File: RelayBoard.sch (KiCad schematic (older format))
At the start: 12 parts

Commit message: Added A New Componet to Relay Lib
* A dioded relay
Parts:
- removed RE1, RE10, RE11, RE12, RE2, RE3, RE4, RE5, RE6, RE7, RE8, RE9: SPST-Relay, symbol SPST-Relay
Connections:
- net labels removed: VCC
- wire segments 15 -> 0
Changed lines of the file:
@@
 LIBS:valves
 LIBS:RelayLib
+LIBS:RelayBoard-cache
 EELAYER 24 0
 EELAYER END
@@
 Comment4 ""
 $EndDescr
-$Comp
-L SPST-Relay RE1
-U 1 1 54E13EE5
-P 1850 1950
-F 0 "RE1" H 1850 1650 60  0000 C CNN
-F 1 "SPST-Relay" H 1850 1850 60  0000 C CNN
-F 2 "" H 1850 1950 60  0000 C CNN
-F 3 "" H 1850 1950 60  0000 C CNN
-	1    1850 1950
-	1    0    0    -1
-$EndComp
-$Comp
-L SPST-Relay RE2
-U 1 1 54E13F01
-P 3150 1950
-F 0 "RE2" H 3150 1650 60  0000 C CNN
-F 1 "SPST-Relay" H 3150 1850 60  0000 C CNN
-F 2 "" H 3150 1950 60  0000 C CNN
-F 3 "" H 3150 1950 60  0000 C CNN
-	1    3150 1950
-	1    0    0    -1
-$EndComp
-$Comp
-L VCC #PWR1
-U 1 1 54E13F0E
-P 800 1650
-F 0 "#PWR1" H 800 1750 30  0001 C CNN
-F 1 "VCC" H 800 1750 30  0000 C CNN
-F 2 "" H 800 1650 60  0000 C CNN
-F 3 "" H 800 1650 60  0000 C CNN
-	1    800  1650
-	1    0    0    -1
-$EndComp
-$Comp
-L SPST-Relay RE3
-U 1 1 54E13F53
-P 4450 1950
-F 0 "RE3" H 4450 1650 60  0000 C CNN
-F 1 "SPST-Relay" H 4450 1850 60  0000 C CNN
-F 2 "" H 4450 1950 60  0000 C CNN
-F 3 "" H 4450 1950 60  0000 C CNN
-	1    4450 1950
-	1    0    0    -1
-$EndComp
-$Comp
-L SPST-Relay RE4
-U 1 1 54E13F5E
-P 5750 1950
-F 0 "RE4" H 5750 1650 60  0000 C CNN
-F 1 "SPST-Relay" H 5750 1850 60  0000 C CNN
-F 2 "" H 5750 1950 60  0000 C CNN
-F 3 "" H 5750 1950 60  0000 C CNN
-	1    5750 1950
-	1    0    0    -1
-$EndComp
-$Comp
-L SPST-Relay RE5
-U 1 1 54E13F69
-P 6950 1950
-F 0 "RE5" H 6950 1650 60  0000 C CNN
-F 1 "SPST-Relay" H 6950 1850 60  0000 C CNN
-F 2 "" H 6950 1950 60  0000 C CNN
-F 3 "" H 6950 1950 60  0000 C CNN
-	1    6950 1950
-	1    0    0    -1
-$EndComp
-$Comp
-L SPST-Relay RE6
-U 1 1 54E14237
-P 8150 1950
-F 0 "RE6" H 8150 1650 60  0000 C CNN
-F 1 "SPST-Relay" H 8150 1850 60  0000 C CNN
-F 2 "" H 8150 1950 60  0000 C CNN
-F 3 "" H 8150 1950 60  0000 C CNN
-	1    8150 1950
-	1    0    0    -1
-$EndComp
-$Comp
-L SPST-Relay RE7
-U 1 1 54E142D7
-P 9350 1950
-F 0 "RE7" H 9350 1650 60  0000 C CNN
-F 1 "SPST-Relay" H 9350 1850 60  0000 C CNN
-F 2 "" H 9350 1950 60  0000 C CNN
-F 3 "" H 9350 1950 60  0000 C CNN
-	1    9350 1950
-	1    0    0    -1
-$EndComp
-$Comp
-L SPST-Relay RE8
-U 1 1 54E142F7
-P 10550 1950
-F 0 "RE8" H 10550 1650 60  0000 C CNN
-F 1 "SPST-Relay" H 10550 1850 60  0000 C CNN
-F 2 "" H 10550 1950 60  0000 C CNN
-F 3 "" H 10550 1950 60  0000 C CNN
-	1    10550 1950
-	1    0    0    -1
-$EndComp
-$Comp
-L SPST-Relay RE9
-U 1 1 54E14302
-P 11750 1950
-F 0 "RE9" H 11750 1650 60  0000 C CNN
-F 1 "SPST-Relay" H 11750 1850 60  0000 C CNN
-F 2 "" H 11750 1950 60  0000 C CNN
-F 3 "" H 11750 1950 60  0000 C CNN
-	1    11750 1950
-	1    0    0    -1
-$EndComp
-$Comp
-L SPST-Relay RE10
-U 1 1 54E1430D
-P 12950 1950
-F 0 "RE10" H 12950 1650 60  0000 C CNN
-F 1 "SPST-Relay" H 12950 1850 60  0000 C CNN
-F 2 "" H 12950 1950 60  0000 C CNN
-F 3 "" H 12950 1950 60  0000 C CNN
-	1    12950 1950
-	1    0    0    -1
-$EndComp
-$Comp
-L SPST-Relay RE11
-U 1 1 54E14318
-P 14150 1950
-F 0 "RE11" H 14150 1650 60  0000 C CNN
-F 1 "SPST-Relay" H 14150 1850 60  0000 C CNN
-F 2 "" H 14150 1950 60  0000 C CNN
-F 3 "" H 14150 1950 60  0000 C CNN
-	1    14150 1950
-	1    0    0    -1
-$EndComp
-$Comp
-L SPST-Relay RE12
-U 1 1 54E14323
-P 15350 1950
-F 0 "RE12" H 15350 1650 60  0000 C CNN
-F 1 "SPST-Relay" H 15350 1850 60  0000 C CNN
-F 2 "" H 15350 1950 60  0000 C CNN
-F 3 "" H 15350 1950 60  0000 C CNN
-	1    15350 1950
-	1    0    0    -1
-$EndComp
-Wire Wire Line
-	800  1650 15850 1650
-Wire Wire Line
-	1200 1650 1200 1900
-Wire Wire Line
-	1200 1900 1350 1900
-Wire Wire Line
-	2650 1650 2650 1900
-Connection ~ 1200 1650
-Wire Wire Line
-	3950 1650 3950 1900
-Connection ~ 2650 1650
-Wire Wire Line
-	5250 1650 5250 1900
-Connection ~ 3950 1650
-Wire Wire Line
-	6450 1650 6450 1900
-Connection ~ 5250 1650
-Wire Wire Line
-	7650 1650 7650 1900
-Connection ~ 6450 1650
-Wire Wire Line
-	8850 1650 8850 1900
-Connection ~ 7650 1650
-Wire Wire Line
-	10050 1650 10050 1900
-Connection ~ 8850 1650
-Wire Wire Line
-	11050 1650 11050 1900
-Connection ~ 10050 1650
-Wire Wire Line
-	12250 1650 12250 1900
-Connection ~ 11050 1650
-Wire Wire Line
-	13450 1650 13450 1900
-Connection ~ 12250 1650
-Wire Wire Line
-	14650 1650 14650 1900
-Connection ~ 13450 1650
-Wire Wire Line
-	15850 1650 15850 1900
-Connection ~ 14650 1650
 $EndSCHEMATC

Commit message: New Componets
* Added Transisters to Diagram
* Wired Diagram
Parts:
- added Q1, Q10, Q11, Q12, Q13, Q14, Q15, Q16, Q2, Q3, Q4, Q5, Q6, Q7, Q8, Q9: NPN, symbol NPN
- added R1, R2: R, symbol R
- added RE1, RE10, RE11, RE12, RE13, RE14, RE15, RE16, RE2, RE3, RE4, RE5, RE6, RE7, RE8, RE9: R-SPDT, symbol R-SPDT
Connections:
- new net: Q1.3 (C), RE1.4
- new net: Q2.3 (C), RE2.4
- new net: Q3.3 (C), RE3.4
- new net: Q4.3 (C), RE4.4
- new net: Q5.3 (C), RE5.4
- new net: Q6.3 (C), RE6.4
- new net: Q7.3 (C), RE7.4
- new net: Q8.3 (C), RE8.4
- new net: Q9.3 (C), RE9.4
- new net: Q10.3 (C), RE10.4
- new net: Q11.3 (C), RE11.4
- new net: Q12.3 (C), RE12.4
- new net: Q13.3 (C), RE13.4
- new net: Q14.3 (C), RE14.4
- new net: Q15.3 (C), RE15.4
- new net: Q16.3 (C), RE16.4
- new net: Q1.2 (B), R1.1
- new net: Q2.2 (B), R2.1
- new net +5V: RE1.5, RE10.5, RE11.5, RE12.5, RE13.5, RE14.5, RE15.5, RE16.5, RE2.5, RE3.5, RE4.5, RE5.5, RE6.5, RE7.5, RE8.5, RE9.5

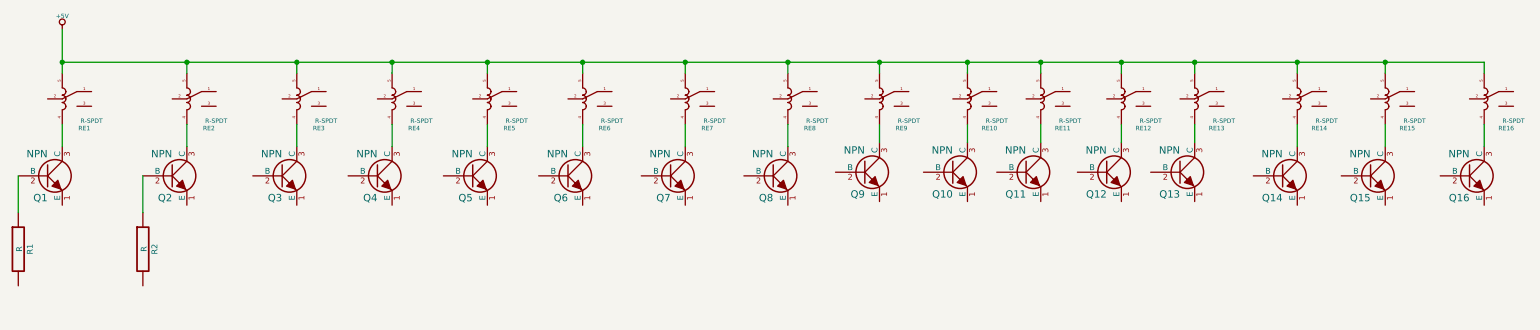
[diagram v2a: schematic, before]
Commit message: Connected to GND
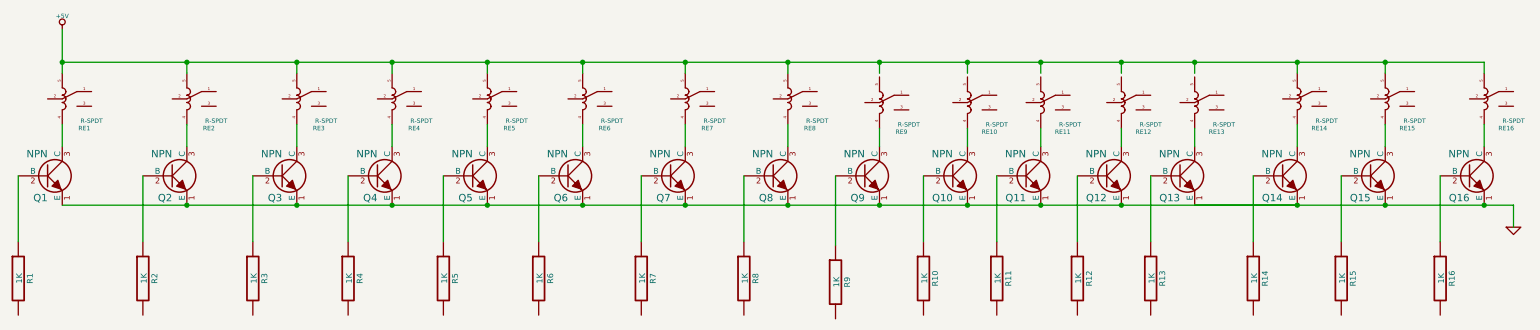
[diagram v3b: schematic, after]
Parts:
- added R10, R11, R12, R13, R14, R15, R16, R3, R4, R5, R6, R7, R8, R9: 1K, symbol R
- R1, R2: value R -> 1K
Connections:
- net labels added: GND
- wire segments 35 -> 52
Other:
- moved on the sheet: Q10, Q11, Q12, Q13, Q9, R1, R2, RE10, RE11, RE12, RE13, RE9

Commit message: Terminal Blocks
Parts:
- added TB? (x6): TermBlk, symbol TermBlk
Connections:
- wire segments 52 -> 66
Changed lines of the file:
@@
-$EndComp
-$Comp
-L +5V #PWR01
-U 1 1 54E16263
-P 1350 925
-F 0 "#PWR01" H 1350 1015 20  0001 C CNN
-F 1 "+5V" H 1350 1015 30  0000 C CNN
-F 2 "" H 1350 925 60  0000 C CNN
-F 3 "" H 1350 925 60  0000 C CNN
-	1    1350 925
-	1    0    0    -1
 $EndComp
 $Comp
@@
 $EndComp
 $Comp
-L GND #PWR02
+L GND #PWR01
 U 1 1 54E16FA4
 P 11250 2275
-F 0 "#PWR02" H 11250 2275 30  0001 C CNN
+F 0 "#PWR01" H 11250 2275 30  0001 C CNN
 F 1 "GND" H 11250 2205 30  0001 C CNN
 F 2 "" H 11250 2275 60  0000 C CNN
@@
 	1    0    0    -1
 $EndComp
-Wire Wire Line
-	1350 925  1350 1225
 Wire Wire Line
 	1350 1150 11050 1150
@@
 Connection ~ 2950 2125
 Connection ~ 2200 2125
+Wire Wire Line
+	1250 1400 1250 1200
+Wire Wire Line
+	1250 1200 1850 1200
+Wire Wire Line
+	1850 1200 1850 1050
+Wire Wire Line
+	1550 1350 1750 1350
+Wire Wire Line
+	1750 1350 1750 1050
+Wire Wire Line
+	1550 1450 1950 1450
+Wire Wire Line
+	1950 1450 1950 1050
+$Comp
+L +5V #PWR02
+U 1 1 54E179BC
+P 1350 875
+F 0 "#PWR02" H 1350 965 20  0001 C CNN
+F 1 "+5V" H 1350 965 30  0000 C CNN
+F 2 "" H 1350 875 60  0000 C CNN
+F 3 "" H 1350 875 60  0000 C CNN
+	1    1350 875
+	1    0    0    -1
+$EndComp
+Wire Wire Line
+	1350 1225 1350 875
+Connection ~ 1350 875
+Wire Wire Line
+	2100 1400 2100 1200
+Wire Wire Line
+	2100 1200 2575 1200
+Wire Wire Line
+	2575 1200 2575 1025
+Wire Wire Line
+	2475 1025 2475 1350
+Wire Wire Line
+	2475 1350 2400 1350
+Wire Wire Line
+	2400 1450 2675 1450
+Wire Wire Line
+	2675 1450 2675 1025
+$Comp
+L TermBlk TB?
+U 1 1 54E17CC8
+P 1850 950
+F 0 "TB?" H 2050 900 60  0000 C CNN
+F 1 "TermBlk" H 1850 1100 60  0000 C CNN
+F 2 "" H 1850 950 60  0000 C CNN
+F 3 "" H 1850 950 60  0000 C CNN
+	1    1850 950
+	1    0    0    -1
+$EndComp
+$Comp
+L TermBlk TB?
+U 1 1 54E17CDC
+P 2575 925
+F 0 "TB?" H 2775 875 60  0000 C CNN
+F 1 "TermBlk" H 2575 1075 60  0000 C CNN
+F 2 "" H 2575 925 60  0000 C CNN
+F 3 "" H 2575 925 60  0000 C CNN
+	1    2575 925
+	1    0    0    -1
+$EndComp
+$Comp
+L TermBlk TB?
+U 1 1 54E17CF0
+P 3325 925
+F 0 "TB?" H 3525 875 60  0000 C CNN
+F 1 "TermBlk" H 3325 1075 60  0000 C CNN
+F 2 "" H 3325 925 60  0000 C CNN
+F 3 "" H 3325 925 60  0000 C CNN
+	1    3325 925
+	1    0    0    -1
+$EndComp
+$Comp
+L TermBlk TB?
+U 1 1 54E17D04
+P 3950 925
+F 0 "TB?" H 4150 875 60  0000 C CNN
+F 1 "TermBlk" H 3950 1075 60  0000 C CNN
+F 2 "" H 3950 925 60  0000 C CNN
+F 3 "" H 3950 925 60  0000 C CNN
+	1    3950 925
+	1    0    0    -1
+$EndComp
+$Comp
+L TermBlk TB?
+U 1 1 54E17D18
+P 4600 925
+F 0 "TB?" H 4800 875 60  0000 C CNN
+F 1 "TermBlk" H 4600 1075 60  0000 C CNN
+F 2 "" H 4600 925 60  0000 C CNN
+F 3 "" H 4600 925 60  0000 C CNN
+	1    4600 925
+	1    0    0    -1
+$EndComp
+$Comp
+L TermBlk TB?
+U 1 1 54E17D2C
+P 5250 925
+F 0 "TB?" H 5450 875 60  0000 C CNN
+F 1 "TermBlk" H 5250 1075 60  0000 C CNN
+F 2 "" H 5250 925 60  0000 C CNN
+F 3 "" H 5250 925 60  0000 C CNN
+	1    5250 925
+	1    0    0    -1
+$EndComp
 $EndSCHEMATC

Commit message: More To The Schematic Than Meets The Eye.
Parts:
- added P1: HE10-32, symbol HE10-32
- added TB10, TB11, TB12, TB13, TB14, TB15, TB16, TB7, TB8, TB9: TermBlk, symbol TermBlk
- gave numbers to parts that had none: 6
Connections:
- net labels added: Pin1, Pin2, Pin3, Pin4, Pin5, Pin6, Pin7
- net labels removed: +5V
- wire segments 66 -> 163

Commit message: End of worktime
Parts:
- added CON1: BARREL_JACK, symbol BARREL_JACK
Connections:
- net GND: now also CON1.2; no longer Q1.1 (E), Q10.1 (E), Q11.1 (E), Q12.1 (E), Q13.1 (E), Q14.1 (E), Q15.1 (E), Q16.1 (E), Q2.1 (E), Q3.1 (E), Q4.1 (E), Q5.1 (E), Q6.1 (E), Q7.1 (E), Q8.1 (E), Q9.1 (E)
- new net: Q1.1 (E), Q10.1 (E), Q11.1 (E), Q12.1 (E), Q13.1 (E), Q14.1 (E), Q15.1 (E), Q16.1 (E), Q2.1 (E), Q3.1 (E), Q4.1 (E), Q5.1 (E), Q6.1 (E), Q7.1 (E), Q8.1 (E), Q9.1 (E)
- new net +5V: CON1.1
- no-connect marks 0 -> 1
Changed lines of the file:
@@
-$EndComp
-$Comp
-L GND #PWR01
-U 1 1 54E16FA4
-P 11250 2275
-F 0 "#PWR01" H 11250 2275 30  0001 C CNN
-F 1 "GND" H 11250 2205 30  0001 C CNN
-F 2 "" H 11250 2275 60  0000 C CNN
-F 3 "" H 11250 2275 60  0000 C CNN
-	1    11250 2275
-	1    0    0    -1
 $EndComp
 $Comp
@@
 Text GLabel 5300 2875 3    60   Input ~ 0
 Pin7
+$Comp
+L BARREL_JACK CON1
+U 1 1 54E1B203
+P 12925 1350
+F 0 "CON1" H 12925 1600 60  0000 C CNN
+F 1 "BARREL_JACK" H 12925 1150 60  0000 C CNN
+F 2 "" H 12925 1350 60  0000 C CNN
+F 3 "" H 12925 1350 60  0000 C CNN
+	1    12925 1350
+	0    1    1    0
+$EndComp
+$Comp
+L GND #PWR01
+U 1 1 54E1B226
+P 12825 1775
+F 0 "#PWR01" H 12825 1775 30  0001 C CNN
+F 1 "GND" H 12825 1705 30  0001 C CNN
+F 2 "" H 12825 1775 60  0000 C CNN
+F 3 "" H 12825 1775 60  0000 C CNN
+	1    12825 1775
+	1    0    0    -1
+$EndComp
+Wire Wire Line
+	12825 1775 12825 1650
+$Comp
+L +5V #PWR02
+U 1 1 54E1B2FB
+P 13200 1650
+F 0 "#PWR02" H 13200 1740 20  0001 C CNN
+F 1 "+5V" H 13200 1740 30  0000 C CNN
+F 2 "" H 13200 1650 60  0000 C CNN
+F 3 "" H 13200 1650 60  0000 C CNN
+	1    13200 1650
+	1    0    0    -1
+$EndComp
+Wire Wire Line
+	13025 1650 13200 1650
+NoConn ~ 12925 1650
 $EndSCHEMATC

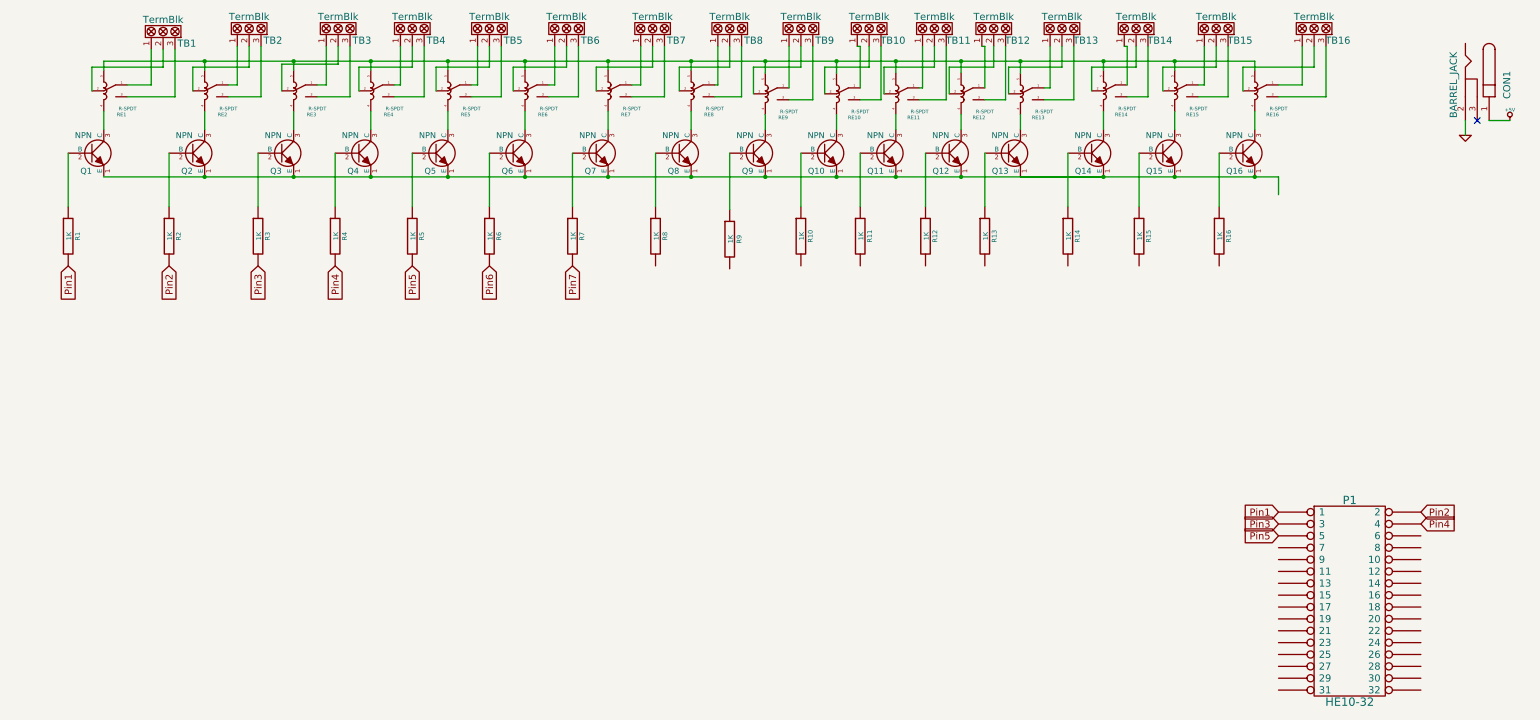
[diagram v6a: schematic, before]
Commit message: Finished Pins 1 to 16 connections
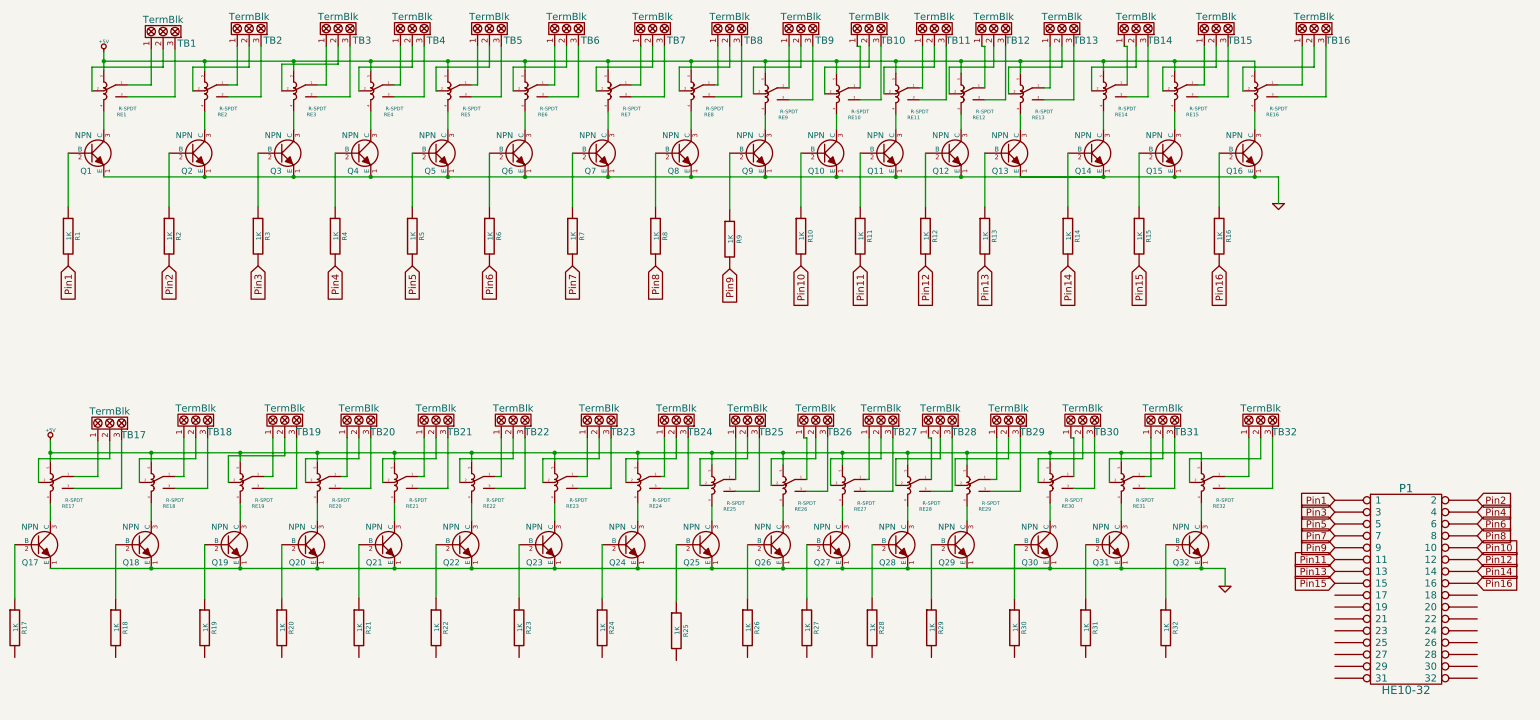
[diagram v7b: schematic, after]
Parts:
- removed CON1: BARREL_JACK, symbol BARREL_JACK
- added Q17, Q18, Q19, Q20, Q21, Q22, Q23, Q24, Q25, Q26, Q27, Q28, Q29, Q30, Q31, Q32: NPN, symbol NPN
- added R17, R18, R19, R20, R21, R22, R23, R24, R25, R26, R27, R28, R29, R30, R31, R32: 1K, symbol R
- added RE17, RE18, RE19, RE20, RE21, RE22, RE23, RE24, RE25, RE26, RE27, RE28, RE29, RE30, RE31, RE32: R-SPDT, symbol R-SPDT
- added TB17, TB18, TB19, TB20, TB21, TB22, TB23, TB24, TB25, TB26, TB27, TB28, TB29, TB30, TB31, TB32: TermBlk, symbol TermBlk
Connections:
- net +5V: now also RE1.5, RE10.5, RE11.5, RE12.5, RE13.5, RE14.5, RE15.5, RE16.5, RE2.5, RE3.5, RE4.5, RE5.5, RE6.5, RE7.5, RE8.5, RE9.5, RE17.5, RE18.5, RE19.5, RE20.5, RE21.5, RE22.5, RE23.5, RE24.5, RE25.5, RE26.5, RE27.5, RE28.5, RE29.5, RE30.5, RE31.5, RE32.5
- net GND: now also Q1.1 (E), Q10.1 (E), Q11.1 (E), Q12.1 (E), Q13.1 (E), Q14.1 (E), Q15.1 (E), Q16.1 (E), Q2.1 (E), Q3.1 (E), Q4.1 (E), Q5.1 (E), Q6.1 (E), Q7.1 (E), Q8.1 (E), Q9.1 (E), Q17.1 (E), Q18.1 (E), Q19.1 (E), Q20.1 (E), Q21.1 (E), Q22.1 (E), Q23.1 (E), Q24.1 (E), Q25.1 (E), Q26.1 (E), Q27.1 (E), Q28.1 (E), Q29.1 (E), Q30.1 (E), Q31.1 (E), Q32.1 (E)
- net Pin6: now also P1.6
- net Pin7: now also P1.7
- net Pin8: now reaches R8.2
- net Pin8: now also P1.8
- net Pin9: now reaches R9.2
- net Pin9: now also P1.9
- net Pin10: now reaches R10.2
- net Pin10: now also P1.10
- net Pin11: now reaches R11.2
- net Pin11: now also P1.11
- net Pin12: now reaches R12.2
- net Pin12: now also P1.12
- net Pin13: now reaches R13.2
- net Pin13: now also P1.13
- net Pin14: now reaches R14.2
- net Pin14: now also P1.14
- net Pin15: now reaches R15.2
- net Pin15: now also P1.15
- net Pin16: now reaches R16.2
- net Pin16: now also P1.16
- new net: RE17.1, TB17.1
- new net: RE17.2, TB17.2
- new net: RE17.3, TB17.3
- new net: Q17.3 (C), RE17.4
- new net: RE18.1, TB18.1
- new net: RE18.2, TB18.2
- new net: RE18.3, TB18.3
- new net: Q18.3 (C), RE18.4
- new net: RE19.1, TB19.1
- new net: RE19.2, TB19.2
- new net: RE19.3, TB19.3
- new net: Q19.3 (C), RE19.4
- new net: RE20.1, TB20.1
- new net: RE20.2, TB20.2
- new net: RE20.3, TB20.3
- new net: Q20.3 (C), RE20.4
- new net: RE21.1, TB21.1
- new net: RE21.2, TB21.2
- new net: RE21.3, TB21.3
- new net: Q21.3 (C), RE21.4
- new net: RE22.1, TB22.1
- new net: RE22.2, TB22.2
- new net: RE22.3, TB22.3
- new net: Q22.3 (C), RE22.4
- new net: RE23.1, TB23.1
- new net: RE23.2, TB23.2
- new net: RE23.3, TB23.3
- new net: Q23.3 (C), RE23.4
- new net: RE24.1, TB24.1
- new net: RE24.2, TB24.2
- new net: RE24.3, TB24.3
- new net: Q24.3 (C), RE24.4
- new net: RE25.1, TB25.1
- new net: RE25.2, TB25.2
- new net: RE25.3, TB25.3
- new net: Q25.3 (C), RE25.4
- new net: RE26.1, TB26.1
- new net: RE26.2, TB26.2
- new net: RE26.3, TB26.3
- new net: Q26.3 (C), RE26.4
- new net: RE27.1, TB27.1
- new net: RE27.2, TB27.2
- new net: RE27.3, TB27.3
- new net: Q27.3 (C), RE27.4
- new net: RE28.1, TB28.1
- new net: RE28.2, TB28.2
- new net: RE28.3, TB28.3
- new net: Q28.3 (C), RE28.4
- new net: RE29.1, TB29.1
- new net: RE29.2, TB29.2
- new net: RE29.3, TB29.3
- new net: Q29.3 (C), RE29.4
- new net: RE30.1, TB30.1
- new net: RE30.2, TB30.2
- new net: RE30.3, TB30.3
- new net: Q30.3 (C), RE30.4
- new net: RE31.1, TB31.1
- new net: RE31.2, TB31.2
- new net: RE31.3, TB31.3
- new net: Q31.3 (C), RE31.4
- new net: RE32.1, TB32.1
- new net: RE32.2, TB32.2
- new net: RE32.3, TB32.3
- new net: Q32.3 (C), RE32.4
- new net: Q17.2 (B), R17.1
- new net: Q18.2 (B), R18.1
- new net: Q19.2 (B), R19.1
- new net: Q20.2 (B), R20.1
- new net: Q21.2 (B), R21.1
- new net: Q22.2 (B), R22.1
- new net: Q23.2 (B), R23.1
- new net: Q24.2 (B), R24.1
- new net: Q25.2 (B), R25.1
- new net: Q26.2 (B), R26.1
- new net: Q27.2 (B), R27.1
- new net: Q28.2 (B), R28.1
- new net: Q29.2 (B), R29.1
- new net: Q30.2 (B), R30.1
- new net: Q32.2 (B), R32.1
- new net: Q31.2 (B), R31.1
- no-connect marks 1 -> 0
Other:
- moved on the sheet: P1
